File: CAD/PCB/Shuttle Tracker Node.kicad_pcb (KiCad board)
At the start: 2 copper layers, 98.9 x 44.1 mm, 27 parts, among them J1 Conn_01x01, J2 Conn_01x01, J3 Conn_01x01, J4 Conn_01x01, J5 Conn_01x01, J6 Conn_01x01, J7 Conn_01x01, SW1 SW_Push, SW10 SW_Push, SW11 SW_Push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

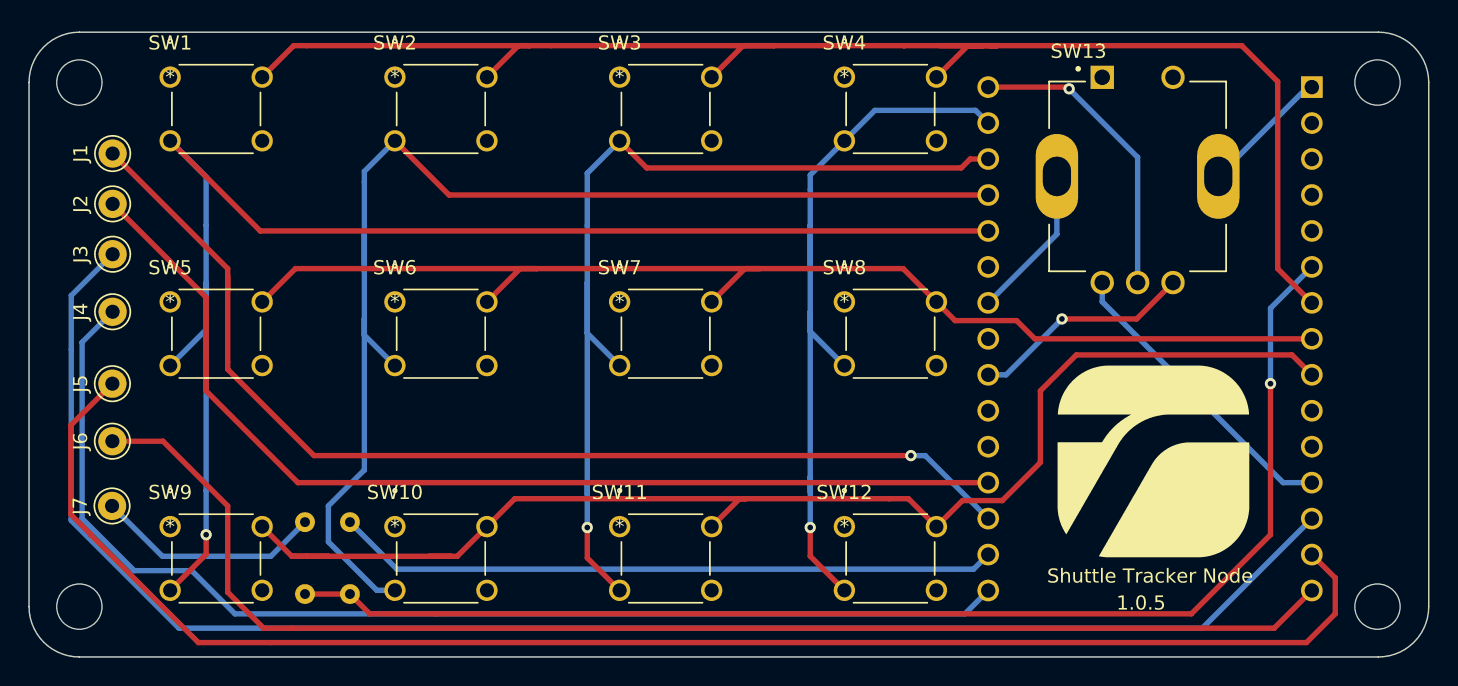
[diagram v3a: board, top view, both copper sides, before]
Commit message: Updated spacing for pins
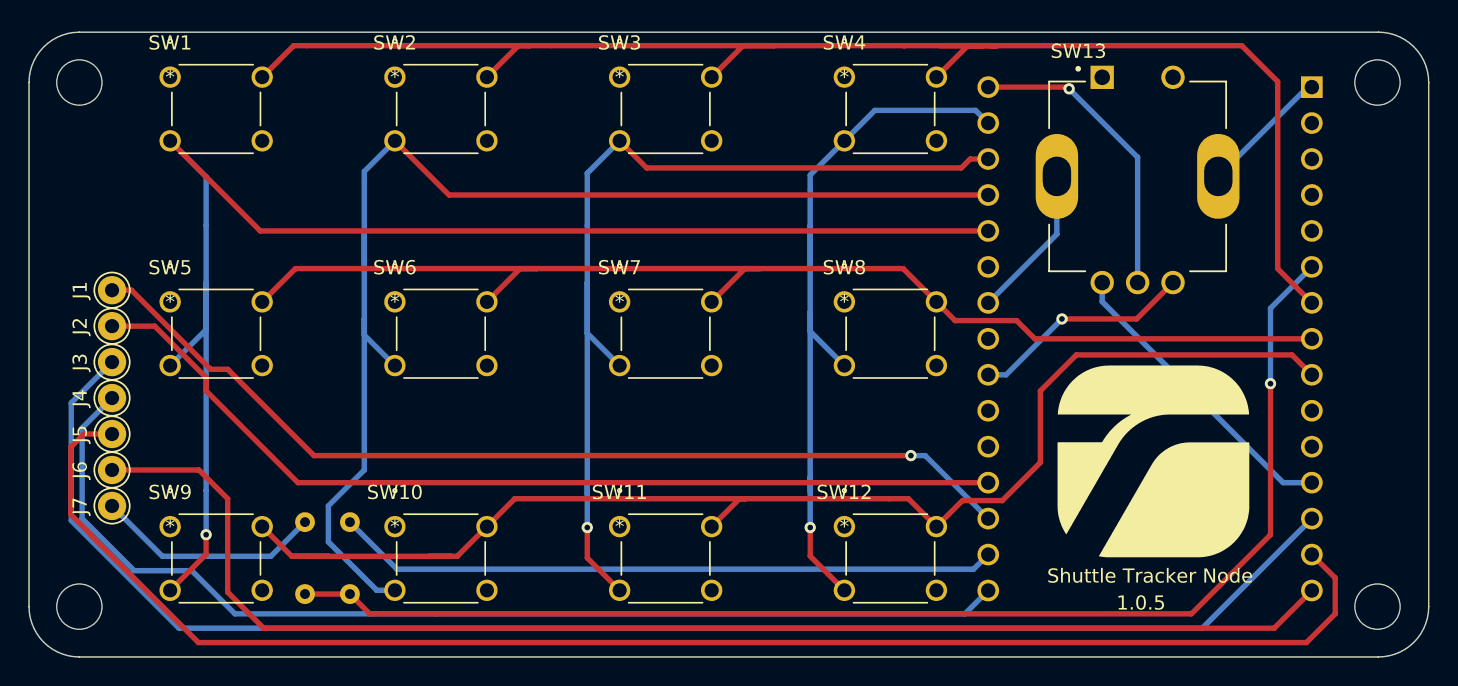
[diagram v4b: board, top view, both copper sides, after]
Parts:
- moved J1 9.65 mm to (135.6, 96.0)
- moved J2 8.64 mm to (135.6, 98.6)
- moved J3 7.62 mm to (135.6, 101.1)
- moved J4 6.10 mm to (135.6, 103.6)
- moved J5 3.56 mm to (135.6, 106.2)
- moved J6 2.03 mm to (135.6, 108.7)
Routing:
- net LCD_DAT: track 77.7 -> 68.6 mm
- net LCD_5V: track 114.0 -> 106.4 mm
- net LCD_CLK: track 73.9 -> 67.0 mm
- net LCD_GND: track 83.0 -> 76.9 mm
- net BAT_5V: track 109.2 -> 106.8 mm
- net BAT_GND: track 94.9 -> 94.3 mm
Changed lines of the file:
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@@
   (net 31 "unconnected-(U1-Pad11)")
   (footprint "Connector_Pin:Pin_D1.0mm_L10.0mm" (layer "F.Cu")
-    (at 135.636 97.536 -90)
+    (at 135.594694 103.632 -90)
     (descr "solder Pin_ diameter 1.0mm, hole diameter 1.0mm (press fit), length 10.0mm")
     (tags "solder Pin_ press fit")
@@
   )
   (footprint "Connector_Pin:Pin_D1.0mm_L10.0mm" (layer "F.Cu")
-    (at 135.636 89.916 -90)
+    (at 135.594694 98.552 -90)
     (descr "solder Pin_ diameter 1.0mm, hole diameter 1.0mm (press fit), length 10.0mm")
     (tags "solder Pin_ press fit")
@@
   )
   (footprint "Connector_Pin:Pin_D1.0mm_L10.0mm" (layer "F.Cu")
-    (at 135.636 93.472 -90)
+    (at 135.594694 101.092 -90)
     (descr "solder Pin_ diameter 1.0mm, hole diameter 1.0mm (press fit), length 10.0mm")
     (tags "solder Pin_ press fit")
@@
   )
   (footprint "Connector_Pin:Pin_D1.0mm_L10.0mm" (layer "F.Cu")
-    (at 135.62 102.616 -90)
+    (at 135.594694 106.172 -90)
     (descr "solder Pin_ diameter 1.0mm, hole diameter 1.0mm (press fit), length 10.0mm")
     (tags "solder Pin_ press fit")
@@
   )
   (footprint "Connector_Pin:Pin_D1.0mm_L10.0mm" (layer "F.Cu")
-    (at 135.62 106.68 -90)
+    (at 135.594694 108.712 -90)
     (descr "solder Pin_ diameter 1.0mm, hole diameter 1.0mm (press fit), length 10.0mm")
     (tags "solder Pin_ press fit")
@@
   )
   (footprint "Connector_Pin:Pin_D1.0mm_L10.0mm" (layer "F.Cu")
-    (at 135.636 86.36 -90)
+    (at 135.594694 96.012 -90)
     (descr "solder Pin_ diameter 1.0mm, hole diameter 1.0mm (press fit), length 10.0mm")
     (tags "solder Pin_ press fit")
@@
     (effects (font (size 1 1) (thickness 0.15)))
   )
-  (segment (start 143.764 94.488) (end 143.764 96.012) (width 0.381) (layer "F.Cu") (net 1))
   (segment (start 149.86 107.696) (end 192.024 107.696) (width 0.381) (layer "F.Cu") (net 1))
-  (segment (start 143.764 101.092) (end 143.764 101.6) (width 0.381) (layer "F.Cu") (net 1))
+  (segment (start 142.555459 101.6) (end 136.967459 96.012) (width 0.381) (layer "F.Cu") (net 1))
   (segment (start 143.764 101.6) (end 149.86 107.696) (width 0.381) (layer "F.Cu") (net 1))
-  (segment (start 143.764 94.996) (end 143.764 96.012) (width 0.381) (layer "F.Cu") (net 1))
-  (segment (start 143.764 96.012) (end 143.764 101.092) (width 0.381) (layer "F.Cu") (net 1))
-  (segment (start 135.636 86.36) (end 143.764 94.488) (width 0.381) (layer "F.Cu") (net 1))
+  (segment (start 143.764 101.6) (end 142.555459 101.6) (width 0.381) (layer "F.Cu") (net 1))
+  (segment (start 136.967459 96.012) (end 135.594694 96.012) (width 0.381) (layer "F.Cu") (net 1))
   (via (at 192.024 107.696) (size 0.8) (drill 0.4) (layers "F.Cu" "B.Cu") (net 1))
   (segment (start 192.024 107.696) (end 193.0332 107.696) (width 0.381) (layer "B.Cu") (net 1))
   (segment (start 193.0332 107.696) (end 197.485 112.1478) (width 0.381) (layer "B.Cu") (net 1))
+  (segment (start 142.24 102.182567) (end 138.609433 98.552) (width 0.381) (layer "F.Cu") (net 2))
   (segment (start 197.485 109.6078) (end 148.7238 109.6078) (width 0.381) (layer "F.Cu") (net 2))
-  (segment (start 142.24 96.52) (end 142.24 98.044) (width 0.381) (layer "F.Cu") (net 2))
+  (segment (start 138.609433 98.552) (end 135.594694 98.552) (width 0.381) (layer "F.Cu") (net 2))
   (segment (start 148.7238 109.6078) (end 142.24 103.124) (width 0.381) (layer "F.Cu") (net 2))
-  (segment (start 135.636 89.916) (end 142.24 96.52) (width 0.381) (layer "F.Cu") (net 2))
-  (segment (start 142.24 103.124) (end 142.24 98.044) (width 0.381) (layer "F.Cu") (net 2))
+  (segment (start 142.24 103.124) (end 142.24 102.182567) (width 0.381) (layer "F.Cu") (net 2))
   (segment (start 132.713091 112.275117) (end 140.325974 119.888) (width 0.381) (layer "B.Cu") (net 3))
   (segment (start 140.325974 119.888) (end 212.6048 119.888) (width 0.381) (layer "B.Cu") (net 3))
-  (segment (start 132.713091 100.201091) (end 132.713091 112.142909) (width 0.381) (layer "B.Cu") (net 3))
-  (segment (start 132.713091 96.394909) (end 132.713091 100.201091) (width 0.381) (layer "B.Cu") (net 3))
-  (segment (start 132.713091 112.142909) (end 132.713091 112.275117) (width 0.381) (layer "B.Cu") (net 3))
-  (segment (start 135.636 93.472) (end 132.713091 96.394909) (width 0.381) (layer "B.Cu") (net 3))
+  (segment (start 132.713091 103.973603) (end 135.594694 101.092) (width 0.381) (layer "B.Cu") (net 3))
+  (segment (start 132.713091 112.275117) (end 132.713091 103.973603) (width 0.381) (layer "B.Cu") (net 3))
   (segment (start 212.6048 119.888) (end 220.345 112.1478) (width 0.381) (layer "B.Cu") (net 3))
   (segment (start 144.272 118.872) (end 195.8408 118.872) (width 0.381) (layer "B.Cu") (net 4))
   (segment (start 141.224 115.824) (end 137.16 115.824) (width 0.381) (layer "B.Cu") (net 4))
+  (segment (start 133.475091 112.139091) (end 133.475091 105.751603) (width 0.381) (layer "B.Cu") (net 4))
   (segment (start 144.272 118.872) (end 141.224 115.824) (width 0.381) (layer "B.Cu") (net 4))
-  (segment (start 133.475091 99.696909) (end 135.636 97.536) (width 0.381) (layer "B.Cu") (net 4))
+  (segment (start 133.475091 105.751603) (end 135.594694 103.632) (width 0.381) (layer "B.Cu") (net 4))
   (segment (start 137.16 115.824) (end 133.475091 112.139091) (width 0.381) (layer "B.Cu") (net 4))
-  (segment (start 133.475091 112.139091) (end 133.475091 99.696909) (width 0.381) (layer "B.Cu") (net 4))
   (segment (start 195.8408 118.872) (end 197.485 117.2278) (width 0.381) (layer "B.Cu") (net 4))
   (segment (start 142.24 114.672501) (end 139.7 117.212501) (width 0.381) (layer "F.Cu") (net 5))
@@
   (segment (start 208.037501 95.475001) (end 208.037501 86.625501) (width 0.381) (layer "B.Cu") (net 28))
   (segment (start 208.037501 86.625501) (end 203.2 81.788) (width 0.381) (layer "B.Cu") (net 28))
-  (segment (start 219.964 120.904) (end 221.996 118.872) (width 0.381) (layer "F.Cu") (net 29))
-  (segment (start 135.62 102.616) (end 132.684681 105.551319) (width 0.381) (layer "F.Cu") (net 29))
-  (segment (start 132.684681 105.551319) (end 132.684681 111.856681) (width 0.381) (layer "F.Cu") (net 29))
-  (segment (start 132.684681 111.856681) (end 134.112 113.284) (width 0.381) (layer "F.Cu") (net 29))
-  (segment (start 134.112 113.284) (end 134.112 113.319435) (width 0.381) (layer "F.Cu") (net 29))
-  (segment (start 141.696565 120.904) (end 146.812 120.904) (width 0.381) (layer "F.Cu") (net 29))
-  (segment (start 134.112 113.319435) (end 141.696565 120.904) (width 0.381) (layer "F.Cu") (net 29))
-  (segment (start 146.812 120.904) (end 219.964 120.904) (width 0.381) (layer "F.Cu") (net 29))
-  (segment (start 221.996 118.872) (end 221.996 116.3388) (width 0.381) (layer "F.Cu") (net 29))
-  (segment (start 221.996 116.3388) (end 220.345 114.6878) (width 0.381) (layer "F.Cu") (net 29))
-  (segment (start 143.764 117.348) (end 146.304 119.888) (width 0.381) (layer "F.Cu") (net 30))
-  (segment (start 139.192 106.68) (end 143.764 111.252) (width 0.381) (layer "F.Cu") (net 30))
-  (segment (start 217.6848 119.888) (end 220.345 117.2278) (width 0.381) (layer "F.Cu") (net 30))
-  (segment (start 143.764 111.252) (end 143.764 117.348) (width 0.381) (layer "F.Cu") (net 30))
-  (segment (start 146.304 119.888) (end 148.336 119.888) (width 0.381) (layer "F.Cu") (net 30))
-  (segment (start 135.62 106.68) (end 139.192 106.68) (width 0.381) (layer "F.Cu") (net 30))
-  (segment (start 148.336 119.888) (end 217.6848 119.888) (width 0.381) (layer "F.Cu") (net 30))
+  (segment (start 141.696565 120.904) (end 134.112 113.319435) (width 0.381) (layer "F.Cu") (net 29))
+  (segment (start 219.964 120.904) (end 141.696565 120.904) (width 0.381) (layer "F.Cu") (net 29))
+  (segment (start 134.112 113.284) (end 132.684681 111.856681) (width 0.381) (layer "F.Cu") (net 29))
+  (segment (start 134.112 113.319435) (end 134.112 113.284) (width 0.381) (layer "F.Cu") (net 29))
+  (segment (start 221.996 116.3388) (end 221.996 118.872) (width 0.381) (layer "F.Cu") (net 29))
+  (segment (start 221.996 118.872) (end 219.964 120.904) (width 0.381) (layer "F.Cu") (net 29))
+  (segment (start 220.345 114.6878) (end 221.996 116.3388) (width 0.381) (layer "F.Cu") (net 29))
+  (segment (start 132.684681 111.856681) (end 132.684681 107.091319) (width 0.381) (layer "F.Cu") (net 29))
+  (segment (start 132.684681 107.091319) (end 133.604 106.172) (width 0.381) (layer "F.Cu") (net 29))
+  (segment (start 133.604 106.172) (end 135.594694 106.172) (width 0.381) (layer "F.Cu") (net 29))
+  (segment (start 220.345 117.2278) (end 217.6848 119.888) (width 0.381) (layer "F.Cu") (net 30))
+  (segment (start 143.764 110.744) (end 141.732 108.712) (width 0.381) (layer "F.Cu") (net 30))
+  (segment (start 146.304 119.888) (end 143.764 117.348) (width 0.381) (layer "F.Cu") (net 30))
+  (segment (start 217.6848 119.888) (end 146.304 119.888) (width 0.381) (layer "F.Cu") (net 30))
+  (segment (start 141.732 108.712) (end 135.594694 108.712) (width 0.381) (layer "F.Cu") (net 30))
+  (segment (start 143.764 117.348) (end 143.764 110.744) (width 0.381) (layer "F.Cu") (net 30))
   (group "" (id 639b4e34-dd1b-4ec8-9119-ffca7ddfe66d)
     (members

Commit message: updated pin configuration for encoder
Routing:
- net ENC_SW_IN: track 10.9 -> 19.9 mm
- net ENC_GND_B: track 9.52 -> 10.7 mm
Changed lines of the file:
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@@
     (fp_circle (center -4.2 -7.6) (end -4.1 -7.6) (layer "F.Fab") (width 0.2) (fill none))
     (fp_circle (center 0 0) (end 3 0) (layer "F.Fab") (width 0.127) (fill none))
-    (pad "1" thru_hole rect (at -2.5 -7) (size 1.65 1.65) (drill 1.1) (layers *.Cu *.Mask))
-    (pad "2" thru_hole circle (at 2.5 -7) (size 1.65 1.65) (drill 1.1) (layers *.Cu *.Mask))
+    (pad "1" thru_hole oval (at -5.7 0) (size 3 6) (drill oval 2 2.8) (layers *.Cu *.Mask))
+    (pad "2" thru_hole oval (at 5.7 0) (size 3 6) (drill oval 2 2.8) (layers *.Cu *.Mask))
     (pad "A" thru_hole circle (at -2.5 7.5) (size 1.65 1.65) (drill 1.1) (layers *.Cu *.Mask)
       (net 12 "ENC_A") (pinfunction "A") (pintype "passive"))
@@
     (pad "C" thru_hole circle (at 0 7.5) (size 1.65 1.65) (drill 1.1) (layers *.Cu *.Mask)
       (net 28 "ENC_GND_A") (pinfunction "C") (pintype "passive"))
-    (pad "S1" thru_hole oval (at -5.7 0) (size 3 6) (drill oval 2 2.8) (layers *.Cu *.Mask)
+    (pad "S1" thru_hole rect (at -2.5 -7) (size 1.65 1.65) (drill 1.1) (layers *.Cu *.Mask)
       (net 14 "ENC_SW_IN") (pinfunction "S1") (pintype "passive"))
-    (pad "S2" thru_hole oval (at 5.7 0) (size 3 6) (drill oval 2 2.8) (layers *.Cu *.Mask)
+    (pad "S2" thru_hole circle (at 2.5 -7) (size 1.65 1.65) (drill 1.1) (layers *.Cu *.Mask)
       (net 15 "ENC_GND_B") (pinfunction "S2") (pintype "passive"))
   )
@@
   (segment (start 202.692 98.044) (end 198.7482 101.9878) (width 0.381) (layer "B.Cu") (net 13))
   (segment (start 198.7482 101.9878) (end 197.485 101.9878) (width 0.381) (layer "B.Cu") (net 13))
-  (segment (start 202.337501 87.975001) (end 202.337501 92.055299) (width 0.381) (layer "B.Cu") (net 14))
-  (segment (start 202.337501 92.055299) (end 197.485 96.9078) (width 0.381) (layer "B.Cu") (net 14))
+  (segment (start 197.485 96.9078) (end 198.566873 96.9078) (width 0.381) (layer "F.Cu") (net 14))
+  (segment (start 198.566873 96.9078) (end 205.537501 89.937172) (width 0.381) (layer "F.Cu") (net 14))
+  (segment (start 205.537501 89.937172) (end 205.537501 80.975001) (width 0.381) (layer "F.Cu") (net 14))
+  (segment (start 210.537501 80.975001) (end 219.652201 80.975001) (width 0.381) (layer "B.Cu") (net 15))
+  (segment (start 219.652201 80.975001) (end 220.345 81.6678) (width 0.381) (layer "B.Cu") (net 15))
   (segment (start 213.737501 87.975001) (end 214.037799 87.975001) (width 0.25) (layer "B.Cu") (net 15))
   (segment (start 220.345 81.6678) (end 220.044702 81.6678) (width 0.381) (layer "B.Cu") (net 15))
-  (segment (start 220.044702 81.6678) (end 213.737501 87.975001) (width 0.381) (layer "B.Cu") (net 15))
   (segment (start 135.594694 111.252) (end 139.150694 114.808) (width 0.381) (layer "B.Cu") (net 21))
   (segment (start 139.150694 114.808) (end 146.812 114.808) (width 0.381) (layer "B.Cu") (net 21))

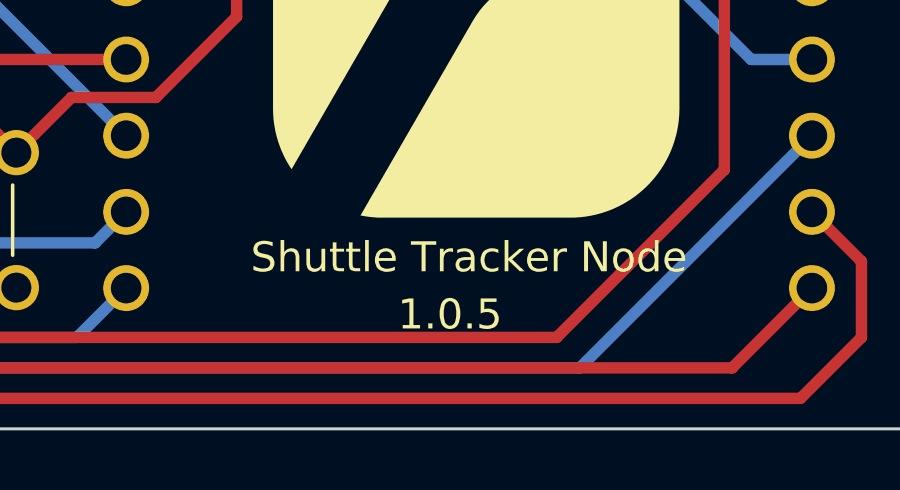
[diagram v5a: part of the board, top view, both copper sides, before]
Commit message: Silkscreen updates
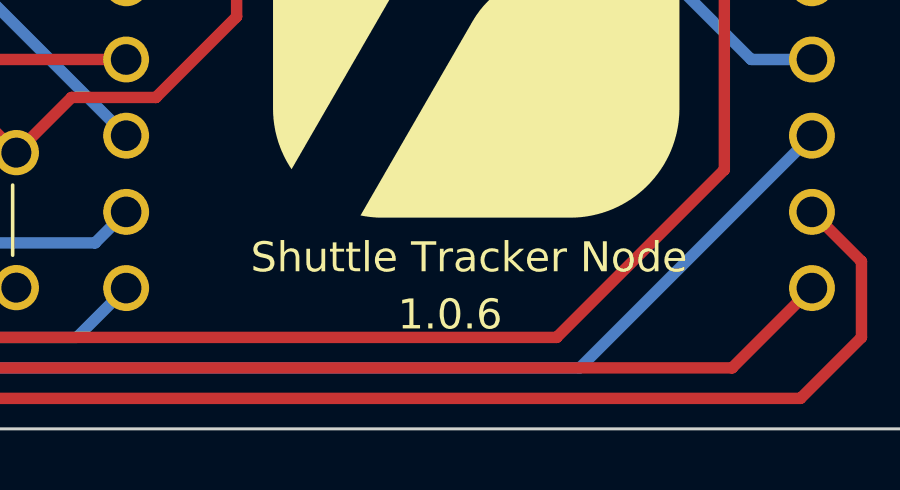
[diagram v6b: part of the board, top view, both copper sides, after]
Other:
- board text added: "1.0.6"
- board text removed: "1.0.5"
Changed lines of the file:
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@@
     (property "Sheetname" "")
     (attr through_hole)
-    (fp_text reference "U1" (at -9.775 21.34) (layer "B.SilkS")
+    (fp_text reference "U1" (at -9.775 21.34) (layer "B.SilkS") hide
       (effects (font (size 1 1) (thickness 0.15)) (justify mirror))
     )
@@
   (gr_line (start 225.044 77.7875) (end 133.2865 77.7875) (layer "Edge.Cuts") (width 0.1))
   (gr_line (start 133.2865 121.92) (end 225.044 121.92) (layer "Edge.Cuts") (width 0.1))
-  (gr_text "1.0.5" (at 208.28 118.11) (layer "F.SilkS")
+  (gr_text "1.0.6" (at 208.28 118.11) (layer "F.SilkS")
     (effects (font (size 1 1) (thickness 0.15)))
   )
@@
   (segment (start 198.566873 96.9078) (end 205.537501 89.937172) (width 0.381) (layer "F.Cu") (net 14))
   (segment (start 205.537501 89.937172) (end 205.537501 80.975001) (width 0.381) (layer "F.Cu") (net 14))
+  (segment (start 213.737501 87.975001) (end 214.037799 87.975001) (width 0.25) (layer "B.Cu") (net 15))
   (segment (start 210.537501 80.975001) (end 219.652201 80.975001) (width 0.381) (layer "B.Cu") (net 15))
+  (segment (start 220.345 81.6678) (end 220.044702 81.6678) (width 0.381) (layer "B.Cu") (net 15))
   (segment (start 219.652201 80.975001) (end 220.345 81.6678) (width 0.381) (layer "B.Cu") (net 15))
-  (segment (start 213.737501 87.975001) (end 214.037799 87.975001) (width 0.25) (layer "B.Cu") (net 15))
-  (segment (start 220.345 81.6678) (end 220.044702 81.6678) (width 0.381) (layer "B.Cu") (net 15))
   (segment (start 135.594694 111.252) (end 139.150694 114.808) (width 0.381) (layer "B.Cu") (net 21))
   (segment (start 139.150694 114.808) (end 146.812 114.808) (width 0.381) (layer "B.Cu") (net 21))
